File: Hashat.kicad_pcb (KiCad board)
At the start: 4 copper layers, 65 x 56.5 mm, 110 parts, among them IC1 BM1397_mode1, J1 Raspberry_Pi_2_3, J2 Conn_01x04, J3 Conn_01x05, Q1 CSD17311Q5, Q2 CSD17311Q5, U10 DS4432U+, U2 LN1134A182MR-G, U3 SN74LVC1T45DBVR, U4 SGM2036-ADJYN5G/TR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

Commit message: finished routing
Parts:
- removed TP2, TP3, TP4: TestPoint, TestPoint:TestPoint_Pad_D1.5mm
- TP1, TP10, TP11, TP12, TP13, TP14, TP15, TP16, TP17, TP18, TP19, TP20, TP23, TP24, TP25, TP32, TP5, TP6, TP7, TP8, TP9: moved to B.Cu
- moved TP1 124.7 mm to (124.0, 95.4), turned to 180 degrees
- moved TP16 123.7 mm to (132.4, 110.0), turned to 180 degrees
- moved TP15 122.6 mm to (128.8, 110.1), turned to 180 degrees
- moved TP12 117.6 mm to (127.9, 97.8), turned to 180 degrees
- moved TP11 116.1 mm to (123.4, 98.7), turned to 180 degrees
- moved TP5 115.4 mm to (110.4, 103.3), turned to 180 degrees
- moved TP24 112.8 mm to (120.7, 102.0), turned to 180 degrees
- moved TP17 112.0 mm to (125.7, 76.8), turned to 180 degrees
- moved TP13 112.0 mm to (128.4, 80.8), turned to 180 degrees
- moved TP14 110.8 mm to (112.8, 105.3), turned to 180 degrees
- moved TP8 109.3 mm to (124.0, 79.0), turned to 180 degrees
- moved TP19 109.3 mm to (114.9, 101.4), turned to 180 degrees
- moved TP7 108.3 mm to (122.7, 76.2), turned to 180 degrees
- moved TP10 105.3 mm to (120.1, 79.1), turned to 180 degrees
- moved TP6 103.1 mm to (114.8, 77.6), turned to 180 degrees
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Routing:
- net GND: track 35.6 -> 70.3 mm, vias 41 -> 56
- net Net-(IC1-NRSTO): track 0.00 -> 12.2 mm, vias 0 -> 1
- net Net-(IC1-CO): track 0.00 -> 10.7 mm, vias 0 -> 1
- net Net-(IC1-BI): track 3.09 -> 12.5 mm
- net Net-(IC1-CLKO): track 0.00 -> 8.50 mm, vias 0 -> 1
- net /3V3: track 8.74 -> 17.1 mm, vias 3 -> 7
- net /Fan/FAN_PWM: track 15.8 -> 23.4 mm, vias 1 -> 2
- net /BM1397/1V8: track 112.5 -> 119.8 mm, vias 8 -> 9
- net Net-(IC1-BO): track 0.00 -> 6.77 mm, vias 0 -> 1
- net Net-(IC1-CLKI): track 4.38 -> 9.68 mm, vias 1 -> 2
- net Net-(IC1-RI): track 6.28 -> 11.4 mm
- net /BM1397/BM_CI: track 14.0 -> 18.9 mm
- net Net-(IC1-PIN_MODE): track 0.00 -> 4.44 mm, vias 0 -> 1
- net /BM1397/0V8: track 47.2 -> 51.3 mm
- net /BM1397/BM_RO: track 24.1 -> 27.8 mm
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
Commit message: got the silkscreen refdes all placed
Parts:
- moved C38 12.0 mm to (93.4, 66.9), turned to 90 degrees
- moved TP19 7.43 mm to (120.7, 106.1)
- moved TP17 3.19 mm to (126.7, 73.8)
- moved TP7 2.50 mm to (123.4, 73.8)
- moved TP23 2.35 mm to (111.5, 73.7)
- moved TP9 2.21 mm to (115.5, 73.8)
- moved TP32 1.36 mm to (119.6, 73.8)
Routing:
- net /Fan/SDA: track 91.3 -> 87.0 mm
- net Net-(IC1-NRSTO): track 12.2 -> 14.9 mm
- net Net-(IC1-CLKO): track 8.50 -> 10.9 mm
- net GND: track 70.3 -> 72.4 mm, vias 56 -> 57
- net /5V: track 146.5 -> 147.9 mm
- net Net-(Q1-G): track 43.6 -> 42.6 mm
- net /BM1397/RO: track 103.8 -> 104.7 mm
- net /BM1397/RST_N: track 93.1 -> 93.8 mm
- net Net-(IC1-RI): track 11.4 -> 12.2 mm
- net /Power/PGOOD: track 5.92 -> 5.21 mm
- net Net-(U9-SS): track 5.43 -> 4.72 mm
- net /BM1397/BM_RST: track 36.1 -> 36.8 mm
- net /BM1397/BM_RO: track 27.8 -> 27.3 mm

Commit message: added sweet graphics
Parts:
- added G***: LOGO, LOGO, F.Cu at (116.1, 64.3)

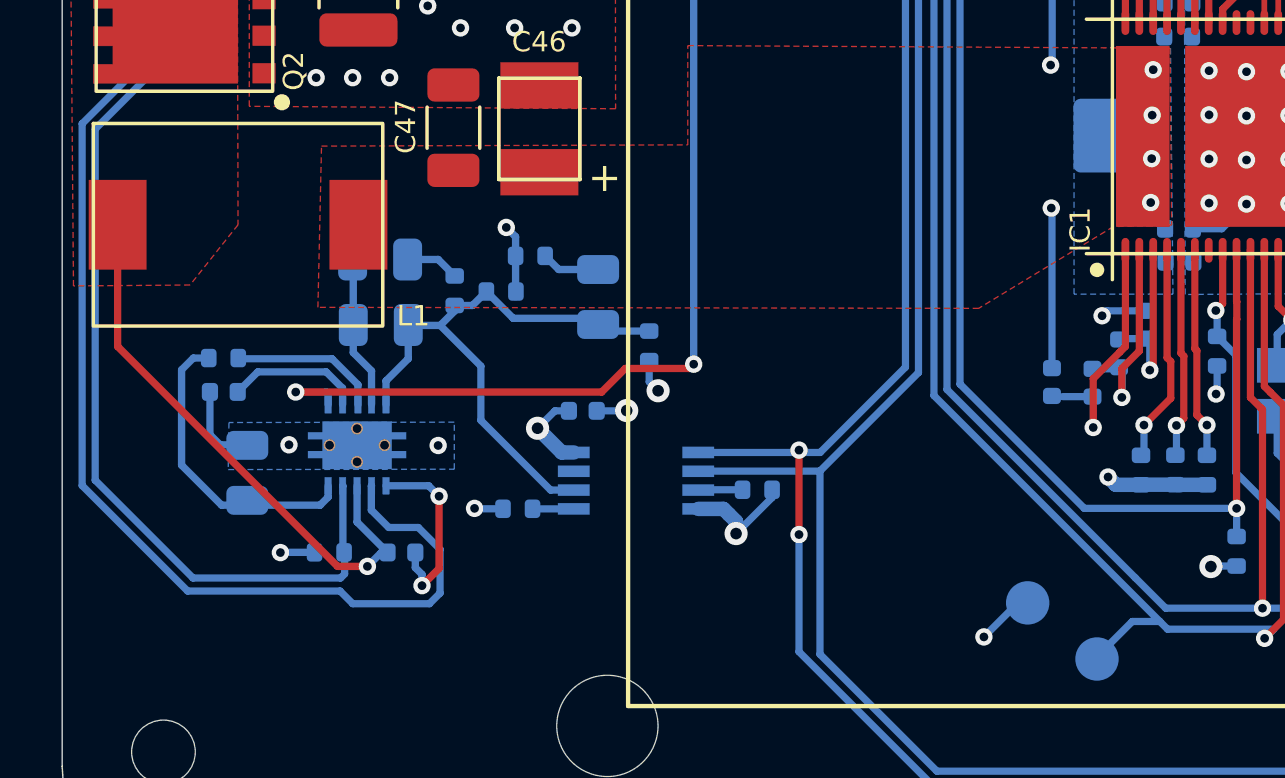
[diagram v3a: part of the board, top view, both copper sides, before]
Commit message: added TPS40305 3d, and Hashat render
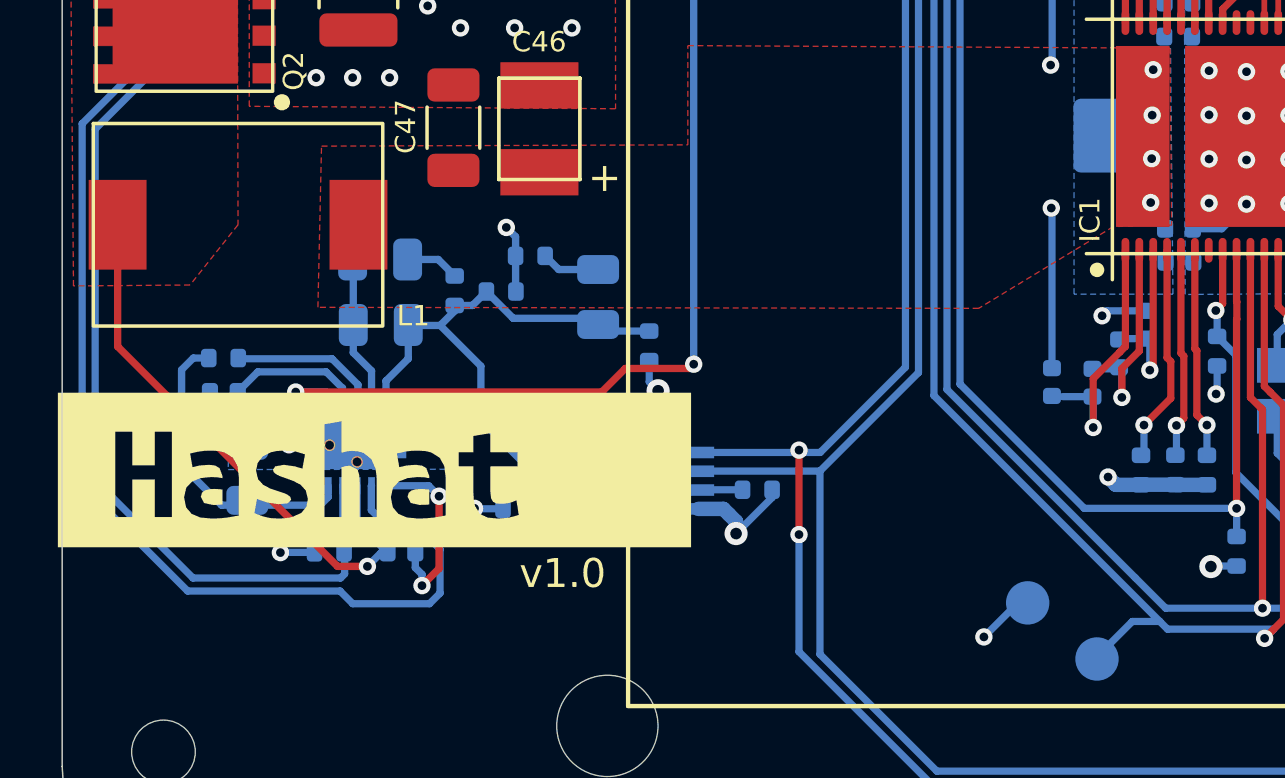
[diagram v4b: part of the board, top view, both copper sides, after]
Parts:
- added kibuzzard-64828601: G***, kibuzzard-64828601, F.Cu at (87.8, 98.8)
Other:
- board text added: "v1.0"
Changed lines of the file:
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@@
     )
   )
+  (footprint "kibuzzard-64828601" (layer "F.Cu")
+    (at 87.791 98.758)
+    (descr "Generated with KiBuzzard")
+    (tags "kb_params=eyJBbGlnbm1lbnRDaG9pY2UiOiAiQ2VudGVyIiwgIkNhcExlZnRDaG9pY2UiOiAiWyIsICJDYXBSaWdodENob2ljZSI6ICJdIiwgIkZvbnRDb21ib0JveCI6ICJVYnVudHVNb25vLUIiLCAiSGVpZ2h0Q3RybCI6ICIzIiwgIkxheWVyQ29tYm9Cb3giOiAiRi5TaWxrUyIsICJNdWx0aUxpbmVUZXh0IjogIkhhc2hhdCIsICJQYWRkaW5nQm90dG9tQ3RybCI6ICI1IiwgIlBhZGRpbmdMZWZ0Q3RybCI6ICIxMCIsICJQYWRkaW5nUmlnaHRDdHJsIjogIjMwIiwgIlBhZGRpbmdUb3BDdHJsIjogIjUiLCAiV2lkdGhDdHJsIjogIiJ9")
+    (attr board_only exclude_from_pos_files exclude_from_bom)
+    (fp_text reference "kibuzzard-64828601" (at 0 -5.718969) (layer "F.SilkS") hide
+        (effects (font (size 0 0) (thickness 0.15)))
+    )
+    (fp_text value "G***" (at 0 5.718969) (layer "F.SilkS") hide
+        (effects (font (size 0 0) (thickness 0.15)))
+    )
+    (fp_poly
+      (pts
+        (xy -5.591969 1.207294)
+        (xy -5.406231 1.204913)
+        (xy -5.249069 1.193006)
+        (xy -5.249069 0.678656)
+        (xy -5.387181 0.661988)
+        (xy -5.534819 0.654844)
+        (xy -5.711031 0.66675)
+        (xy -5.86105 0.707231)
+        (xy -5.963444 0.788194)
+        (xy -6.001544 0.926306)
+        (xy -5.887244 1.143)
+        (xy -5.591969 1.207294)
+      )
+      (stroke (width 0) (type solid)) (fill solid) (layer "F.SilkS"))
+    (fp_poly
+      (pts
+        (xy 1.551781 1.207294)
+        (xy 1.737519 1.204913)
+        (xy 1.894681 1.193006)
+        (xy 1.894681 0.678656)
+        (xy 1.756569 0.661988)
+        (xy 1.608931 0.654844)
+        (xy 1.432719 0.66675)
+        (xy 1.2827 0.707231)
+        (xy 1.180306 0.788194)
+        (xy 1.142206 0.926306)
+        (xy 1.256506 1.143)
+        (xy 1.551781 1.207294)
+      )
+      (stroke (width 0) (type solid)) (fill solid) (layer "F.SilkS"))
+    (fp_poly
+      (pts
+        (xy -8.954294 -2.670969)
+        (xy -10.938669 -2.670969)
+        (xy -10.938669 2.670969)
+        (xy -8.954294 2.670969)
+        (xy -7.001669 2.670969)
+        (xy -7.001669 1.626394)
+        (xy -7.587456 1.626394)
+        (xy -7.587456 0.326231)
+        (xy -8.368506 0.326231)
+        (xy -8.368506 1.626394)
+        (xy -8.954294 1.626394)
+        (xy -8.954294 -1.321594)
+        (xy -8.368506 -1.321594)
+        (xy -8.368506 -0.159544)
+        (xy -7.587456 -0.159544)
+        (xy -7.587456 -1.321594)
+        (xy -7.001669 -1.321594)
+        (xy -7.001669 1.626394)
+        (xy -7.001669 2.670969)
+        (xy -5.634831 2.670969)
+        (xy -5.634831 1.678781)
+        (xy -6.022975 1.640681)
+        (xy -6.320631 1.514475)
+        (xy -6.511131 1.285875)
+        (xy -6.577806 0.940594)
+        (xy -6.501606 0.611981)
+        (xy -6.296819 0.397669)
+        (xy -6.001544 0.280987)
+        (xy -5.653881 0.245269)
+        (xy -5.438378 0.254794)
+        (xy -5.249069 0.283369)
+        (xy -5.249069 0.211931)
+        (xy -5.353844 -0.066675)
+        (xy -5.496719 -0.150614)
+        (xy -5.715794 -0.178594)
+        (xy -6.037263 -0.154781)
+        (xy -6.287294 -0.097631)
+        (xy -6.368256 -0.569119)
+        (xy -6.058694 -0.638175)
+        (xy -5.855097 -0.661392)
+        (xy -5.644356 -0.669131)
+        (xy -5.391348 -0.653058)
+        (xy -5.184775 -0.604838)
+        (xy -4.891881 -0.423863)
+        (xy -4.734719 -0.138112)
+        (xy -4.687094 0.240506)
+        (xy -4.687094 1.574006)
+        (xy -5.068094 1.640681)
+        (xy -5.335984 1.669256)
+        (xy -5.634831 1.678781)
+        (xy -5.634831 2.670969)
+        (xy -3.325019 2.670969)
+        (xy -3.325019 1.678781)
+        (xy -3.5941 1.662112)
+        (xy -3.820319 1.612106)
+        (xy -4.148931 1.493044)
+        (xy -4.058444 1.002506)
+        (xy -3.703638 1.126331)
+        (xy -3.320256 1.183481)
+        (xy -2.991644 1.152525)
+        (xy -2.877344 1.026319)
+        (xy -2.913062 0.921544)
+        (xy -3.013075 0.847725)
+        (xy -3.160713 0.788194)
+        (xy -3.334544 0.731044)
+        (xy -3.596481 0.642938)
+        (xy -3.839369 0.516731)
+        (xy -4.020344 0.32385)
+        (xy -4.091781 0.030956)
+        (xy -4.037013 -0.238125)
+        (xy -3.865563 -0.461963)
+        (xy -3.567906 -0.614363)
+        (xy -3.369072 -0.655439)
+        (xy -3.134519 -0.669131)
+        (xy -2.923183 -0.660797)
+        (xy -2.727325 -0.635794)
+        (xy -2.401094 -0.540544)
+        (xy -2.491581 -0.045244)
+        (xy -2.743994 -0.123825)
+        (xy -3.129756 -0.178594)
+        (xy -3.432175 -0.123825)
+        (xy -3.510756 -0.007144)
+        (xy -3.475038 0.085725)
+        (xy -3.379788 0.159544)
+        (xy -3.241675 0.223837)
+        (xy -3.072606 0.283369)
+        (xy -2.805906 0.378619)
+        (xy -2.555875 0.509587)
+        (xy -2.372519 0.709612)
+        (xy -2.301081 1.007269)
+        (xy -2.353469 1.269206)
+        (xy -2.5273 1.483519)
+        (xy -2.844006 1.626394)
+        (xy -3.061891 1.665684)
+        (xy -3.325019 1.678781)
+        (xy -3.325019 2.670969)
+        (xy -1.724819 2.670969)
+        (xy -1.724819 1.626394)
+        (xy -1.724819 -1.578769)
+        (xy -1.139031 -1.678781)
+        (xy -1.139031 -0.592931)
+        (xy -0.967581 -0.638175)
+        (xy -0.791369 -0.659606)
+        (xy -0.563959 -0.641152)
+        (xy -0.377031 -0.585787)
+        (xy -0.110331 -0.376238)
+        (xy 0.032544 -0.052388)
+        (xy 0.064691 0.145852)
+        (xy 0.075406 0.364331)
+        (xy 0.075406 1.626394)
+        (xy -0.510381 1.626394)
+        (xy -0.510381 0.440531)
+        (xy -0.528241 0.170259)
+        (xy -0.581819 -0.011906)
+        (xy -0.853281 -0.150019)
+        (xy -1.012825 -0.130969)
+        (xy -1.139031 -0.097631)
+        (xy -1.139031 1.626394)
+        (xy -1.724819 1.626394)
+        (xy -1.724819 2.670969)
+        (xy 1.508919 2.670969)
+        (xy 1.508919 1.678781)
+        (xy 1.120775 1.640681)
+        (xy 0.823119 1.514475)
+        (xy 0.632619 1.285875)
+        (xy 0.565944 0.940594)
+        (xy 0.642144 0.611981)
+        (xy 0.846931 0.397669)
+        (xy 1.142206 0.280987)
+        (xy 1.489869 0.245269)
+        (xy 1.705372 0.254794)
+        (xy 1.894681 0.283369)
+        (xy 1.894681 0.211931)
+        (xy 1.789906 -0.066675)
+        (xy 1.647031 -0.150614)
+        (xy 1.427956 -0.178594)
+        (xy 1.106488 -0.154781)
+        (xy 0.856456 -0.097631)
+        (xy 0.775494 -0.569119)
+        (xy 1.085056 -0.638175)
+        (xy 1.288653 -0.661392)
+        (xy 1.499394 -0.669131)
+        (xy 1.752402 -0.653058)
+        (xy 1.958975 -0.604838)
+        (xy 2.251869 -0.423863)
+        (xy 2.409031 -0.138112)
+        (xy 2.456656 0.240506)
+        (xy 2.456656 1.574006)
+        (xy 2.075656 1.640681)
+        (xy 1.807766 1.669256)
+        (xy 1.508919 1.678781)
+        (xy 1.508919 2.670969)
+        (xy 4.271169 2.670969)
+        (xy 4.271169 1.678781)
+        (xy 3.909219 1.645444)
+        (xy 3.642519 1.516856)
+        (xy 3.475831 1.247775)
+        (xy 3.432969 1.047155)
+        (xy 3.418681 0.792956)
+        (xy 3.418681 -0.126206)
+        (xy 2.909094 -0.126206)
+        (xy 2.909094 -0.611981)
+        (xy 3.418681 -0.611981)
+        (xy 3.418681 -1.173956)
+        (xy 4.004469 -1.269206)
+        (xy 4.004469 -0.611981)
+        (xy 4.942681 -0.611981)
+        (xy 4.942681 -0.126206)
+        (xy 4.004469 -0.126206)
+        (xy 4.004469 0.778669)
+        (xy 4.028281 0.978694)
+        (xy 4.094956 1.097756)
+        (xy 4.199731 1.154906)
+        (xy 4.337844 1.169194)
+        (xy 4.487862 1.164431)
+        (xy 4.621213 1.147763)
+        (xy 4.754563 1.112044)
+        (xy 4.904581 1.050131)
+        (xy 4.985544 1.554956)
+        (xy 4.6355 1.650206)
+        (xy 4.271169 1.678781)
+        (xy 4.271169 2.670969)
+        (xy 4.985544 2.670969)
+        (xy 10.938669 2.670969)
+        (xy 10.938669 -2.670969)
+        (xy 4.985544 -2.670969)
+        (xy -8.954294 -2.670969)
+      )
+      (stroke (width 0) (type solid)) (fill solid) (layer "F.SilkS"))
+  )
   (footprint "bitaxe:BM1397" (layer "F.Cu")
     (at 117.3364 87.234 90)
@@
     (property "Sheetfile" "bm1397.kicad_sch")
     (property "Sheetname" "BM1397")
-    (fp_text reference "IC1" (at -4 -4.749 90) (layer "F.SilkS")
+    (fp_text reference "IC1" (at -3.666 -4.4114 90) (layer "F.SilkS")
         (effects (font (size 0.7 0.7) (thickness 0.1)) (justify left bottom))
     )
@@
   (gr_arc (start 80 112) (mid 77.87868 111.12132) (end 77 109)
     (stroke (width 0.05) (type solid)) (layer "Edge.Cuts"))
+  (gr_text "v1.0" (at 92.797 102.922) (layer "F.SilkS")
+    (effects (font (size 1 1) (thickness 0.15)) (justify left bottom))
+  )
   (segment (start 93.398 65.976) (end 92.085 65.976) (width 0.5) (layer "F.Cu") (net 1))
   (segment (start 119.9764 81.742026) (end 119.9764 83.2994) (width 0.25) (layer "F.Cu") (net 1))

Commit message: trace massaging
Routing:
- net unconnected-(IC1-TEST-Pad7): track 0.00 -> 0.87 mm
- net unconnected-(IC1-TF-Pad24): track 0.00 -> 0.75 mm
- net unconnected-(IC1-RF-Pad23): track 0.00 -> 0.74 mm
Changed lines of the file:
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@@
   (segment (start 93.398 65.976) (end 92.085 65.976) (width 0.5) (layer "F.Cu") (net 1))
   (segment (start 119.9764 81.742026) (end 119.9764 83.2994) (width 0.25) (layer "F.Cu") (net 1))
+  (segment (start 119.672 92.76) (end 119.4964 92.5844) (width 0.25) (layer "F.Cu") (net 1))
   (segment (start 92.085 65.976) (end 91.554 65.445) (width 0.5) (layer "F.Cu") (net 1))
   (segment (start 120.188381 81.530045) (end 119.9764 81.742026) (width 0.25) (layer "F.Cu") (net 1))
-  (segment (start 119.4964 91.1686) (end 119.4964 92.1944) (width 0.25) (layer "F.Cu") (net 1))
-  (segment (start 119.4964 92.1944) (end 119.681 92.379) (width 0.25) (layer "F.Cu") (net 1))
+  (segment (start 119.4964 92.5844) (end 119.4964 91.1686) (width 0.25) (layer "F.Cu") (net 1))
   (via (at 108.847 104.527) (size 0.6) (drill 0.3) (layers "F.Cu" "B.Cu") (net 1))
   (via (at 90.763745 81.944278) (size 0.6) (drill 0.3) (layers "F.Cu" "B.Cu") (net 1))
@@
   (via (at 89.63 82.723) (size 0.6) (drill 0.3) (layers "F.Cu" "B.Cu") (net 1))
   (via (at 91.249 100.085) (size 0.6) (drill 0.3) (layers "F.Cu" "B.Cu") (net 1))
-  (via (at 119.681 92.379) (size 0.6) (drill 0.3) (layers "F.Cu" "B.Cu") (net 1))
+  (via (at 119.672 92.76) (size 0.6) (drill 0.3) (layers "F.Cu" "B.Cu") (net 1))
   (via (at 120.682 84.964) (size 0.6) (drill 0.3) (layers "F.Cu" "B.Cu") (net 1))
   (via (at 117.921 88.046666) (size 0.6) (drill 0.3) (layers "F.Cu" "B.Cu") (net 1))
@@
   (segment (start 121.337604 93.608) (end 124.138396 93.608) (width 0.25) (layer "F.Cu") (net 36))
   (segment (start 124.4025 81.0665) (end 122.872 81.0665) (width 0.25) (layer "F.Cu") (net 36))
-  (segment (start 119.9764 91.1686) (end 119.9764 91.791) (width 0.25) (layer "F.Cu") (net 36))
   (segment (start 126.717 88.967) (end 126.717 85.08) (width 0.25) (layer "F.Cu") (net 36))
   (segment (start 126.717 85.08) (end 126.717 83.381) (width 0.25) (layer "F.Cu") (net 36))
+  (segment (start 119.9764 91.1686) (end 119.9764 92.1404) (width 0.25) (layer "F.Cu") (net 36))
+  (segment (start 120.107 92.271) (end 120.4564 92.271) (width 0.25) (layer "F.Cu") (net 36))
   (segment (start 120.4564 82.145204) (end 121.535104 81.0665) (width 0.25) (layer "F.Cu") (net 36))
   (segment (start 125.94 88.967) (end 126.717 88.967) (width 0.25) (layer "F.Cu") (net 36))
+  (segment (start 119.9764 92.1404) (end 120.107 92.271) (width 0.25) (layer "F.Cu") (net 36))
   (segment (start 121.535104 81.0665) (end 122.872 81.0665) (width 0.25) (layer "F.Cu") (net 36))
   (segment (start 120.4564 92.726796) (end 121.337604 93.608) (width 0.25) (layer "F.Cu") (net 36))
@@
   (segment (start 124.138396 93.608) (end 126.717 91.029396) (width 0.25) (layer "F.Cu") (net 36))
   (segment (start 120.4564 83.2994) (end 120.4564 82.145204) (width 0.25) (layer "F.Cu") (net 36))
-  (segment (start 119.9764 91.791) (end 120.4564 92.271) (width 0.25) (layer "F.Cu") (net 36))
   (segment (start 125.9165 85.095) (end 126.702 85.095) (width 0.25) (layer "F.Cu") (net 36))
   (segment (start 126.717 83.381) (end 124.4025 81.0665) (width 0.25) (layer "F.Cu") (net 36))
@@
   (via (at 116.554 97.207) (size 0.6) (drill 0.3) (layers "F.Cu" "B.Cu") (net 43))
   (segment (start 116.554 97.207) (end 116.554 98.251) (width 0.25) (layer "B.Cu") (net 43))
+  (segment (start 116.6164 91.1686) (end 116.6164 92.0264) (width 0.25) (layer "F.Cu") (net 44))
+  (segment (start 116.6164 92.0264) (end 116.622 92.032) (width 0.25) (layer "F.Cu") (net 44))
   (segment (start 117.0964 93.0135) (end 117.0964 91.1686) (width 0.25) (layer "F.Cu") (net 45))
   (segment (start 116.8609 93.249) (end 117.0964 93.0135) (width 0.25) (layer "F.Cu") (net 45))
@@
   (segment (start 125.196 97.570794) (end 125.196 98.822) (width 0.2) (layer "B.Cu") (net 48))
   (segment (start 125.108 98.734) (end 125.196 98.822) (width 0.2) (layer "B.Cu") (net 48))
-  (segment (start 117.9369 82.016) (end 117.914262 82.016) (width 0.25) (layer "F.Cu") (net 51))
-  (segment (start 117.914262 82.016) (end 117.0964 82.833862) (width 0.25) (layer "F.Cu") (net 51))
-  (segment (start 117.0964 82.833862) (end 117.0964 83.2994) (width 0.25) (layer "F.Cu") (net 51))
-  (via (at 117.9369 82.016) (size 0.6) (drill 0.3) (layers "F.Cu" "B.Cu") (net 51))
+  (segment (start 118.058 83.2978) (end 118.058 82.561) (width 0.25) (layer "F.Cu") (net 49))
+  (segment (start 118.058 82.561) (end 118.06 82.559) (width 0.25) (layer "F.Cu") (net 49))
+  (segment (start 118.0564 83.2994) (end 118.058 83.2978) (width 0.25) (layer "F.Cu") (net 49))
+  (segment (start 117.5764 82.5484) (end 117.574 82.546) (width 0.25) (layer "F.Cu") (net 50))
+  (segment (start 117.5764 83.2994) (end 117.5764 82.5484) (width 0.25) (layer "F.Cu") (net 50))
+  (segment (start 117.0964 82.1976) (end 117.0964 83.2994) (width 0.25) (layer "F.Cu") (net 51))
+  (segment (start 117.722723 81.571277) (end 117.0964 82.1976) (width 0.25) (layer "F.Cu") (net 51))
+  (segment (start 117.9369 81.571277) (end 117.722723 81.571277) (width 0.25) (layer "F.Cu") (net 51))
+  (via (at 117.9369 81.571277) (size 0.6) (drill 0.3) (layers "F.Cu" "B.Cu") (net 51))
+  (segment (start 116.488 80.501) (end 116.488 74.716) (width 0.25) (layer "B.Cu") (net 51))
   (segment (start 116.488 74.716) (end 115.543 73.771) (width 0.25) (layer "B.Cu") (net 51))
-  (segment (start 117.9369 82.016) (end 117.9369 81.9499) (width 0.25) (layer "B.Cu") (net 51))
-  (segment (start 116.488 80.501) (end 116.488 74.716) (width 0.25) (layer "B.Cu") (net 51))
-  (segment (start 117.9369 81.9499) (end 116.488 80.501) (width 0.25) (layer "B.Cu") (net 51))
+  (segment (start 117.9369 81.571277) (end 117.558277 81.571277) (width 0.25) (layer "B.Cu") (net 51))
+  (segment (start 117.558277 81.571277) (end 116.488 80.501) (width 0.25) (layer "B.Cu") (net 51))
   (segment (start 118.1114 80.5136) (end 118.1114 80.2446) (width 0.25) (layer "F.Cu") (net 52))
   (segment (start 118.1114 80.2446) (end 120.107 78.249) (width 0.25) (layer "F.Cu") (net 52))
